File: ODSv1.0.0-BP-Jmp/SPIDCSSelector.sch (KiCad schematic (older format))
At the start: 4 parts, among them U1 MAX7317, U2 74HC4067PW

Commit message: Disconnect BT & BP-Jmp backbone MAX7317 DOUT (#16); make DOUT output pin
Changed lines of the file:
@@
 $Descr USLetter 11000 8500
 encoding utf-8
-Sheet 3 9
+Sheet 4 9
 Title "Breakout Plane for Jumper Wires"
 Date "2021-03-09"
@@
 Text HLabel 1000 2050 0    50   Input ~ 0
 COPI
-Text HLabel 1000 2150 0    50   3State ~ 0
-CIPO
 Text HLabel 1000 2250 0    50   Input ~ 0
 ~DSCS~
@@
 Text HLabel 3500 1000 1    50   Input ~ 0
 3.3V
+Text HLabel 1000 2150 0    50   Output ~ 0
+CIPO
 $EndSCHEMATC

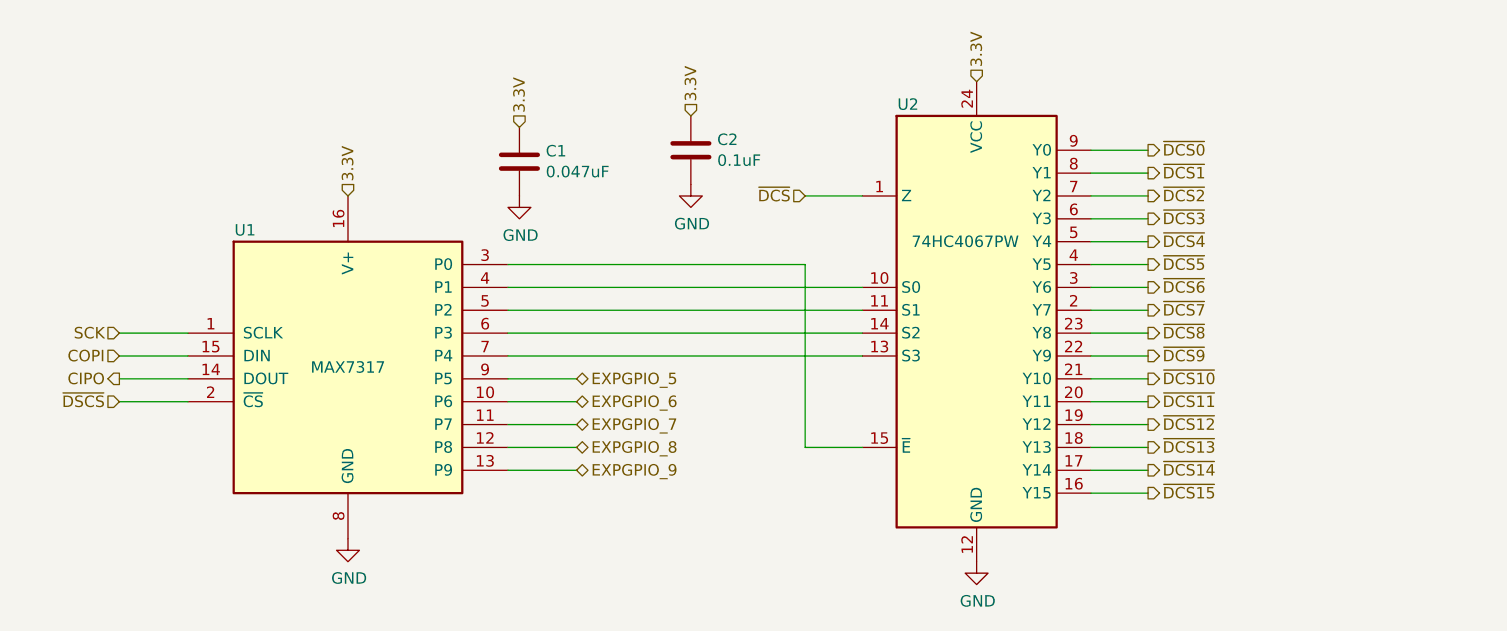
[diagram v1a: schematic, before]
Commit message: Insert 3-state buffers between all MAX7317 DOUTs and CIPO (#16)
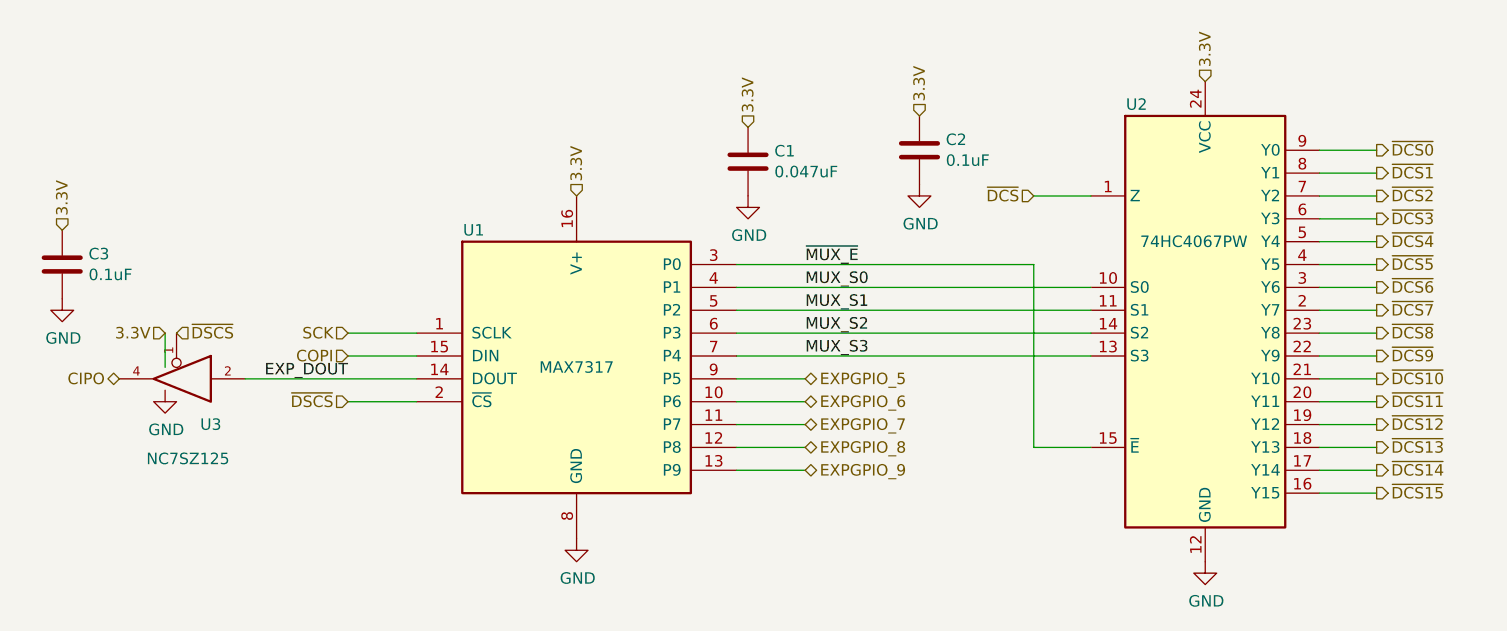
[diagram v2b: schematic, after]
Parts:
- added C3: 0.1uF, Capacitor_SMD:C_0603_1608Metric, symbol Device:C
- added U3: NC7SZ125, Package_TO_SOT_SMD:SOT-353_SC-70-5, symbol Octopi:NC7SZ125
- C1, C2, U1, U2: Config -NoIC -> (none)
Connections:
- net CIPO: now also U3.4; no longer U1.14 (DOUT)
- net GND: now also C3.2, U3.3 (GND)
- net ~DSCS~: now also U3.1
- net ~MUX_E~: now reaches U1.3 (P0), U2.15 (~E)
- net MUX_S0: now reaches U1.4 (P1), U2.10 (S0)
- net MUX_S1: now reaches U1.5 (P2), U2.11 (S1)
- net MUX_S2: now reaches U1.6 (P3), U2.14 (S2)
- net MUX_S3: now reaches U1.7 (P4), U2.13 (S3)
- net 3.3V renamed VCC
- net VCC: now also C3.1, U3.5 (VCC)
- new net EXP_DOUT: U1.14 (DOUT), U3.2
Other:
- moved on the sheet: C1, C2, U1, U2
